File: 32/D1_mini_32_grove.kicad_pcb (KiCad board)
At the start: 2 copper layers, 3 parts, among them J1 Conn_01x04_Pin, J2 Conn_01x04_Pin, U1 esp32-wemos-d1-mini

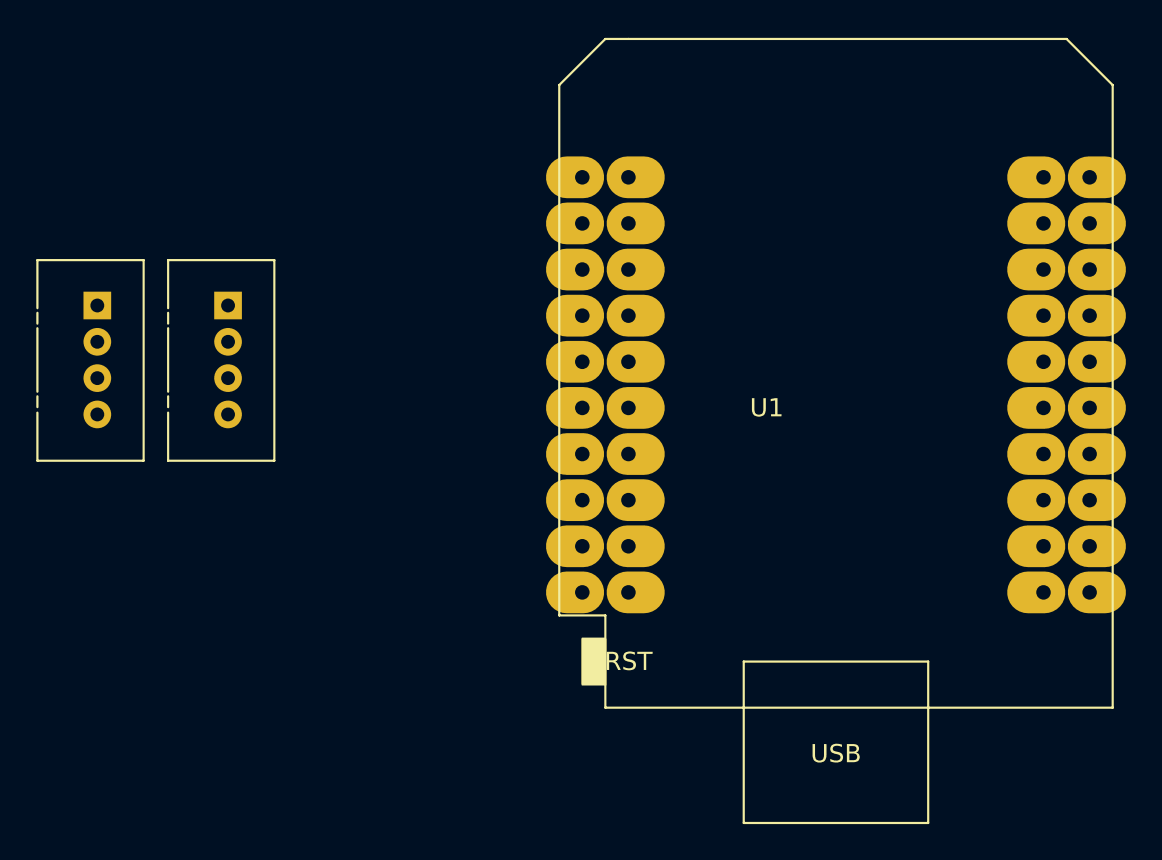
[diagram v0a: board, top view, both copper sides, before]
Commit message: First draft of 32 board ready for testrun
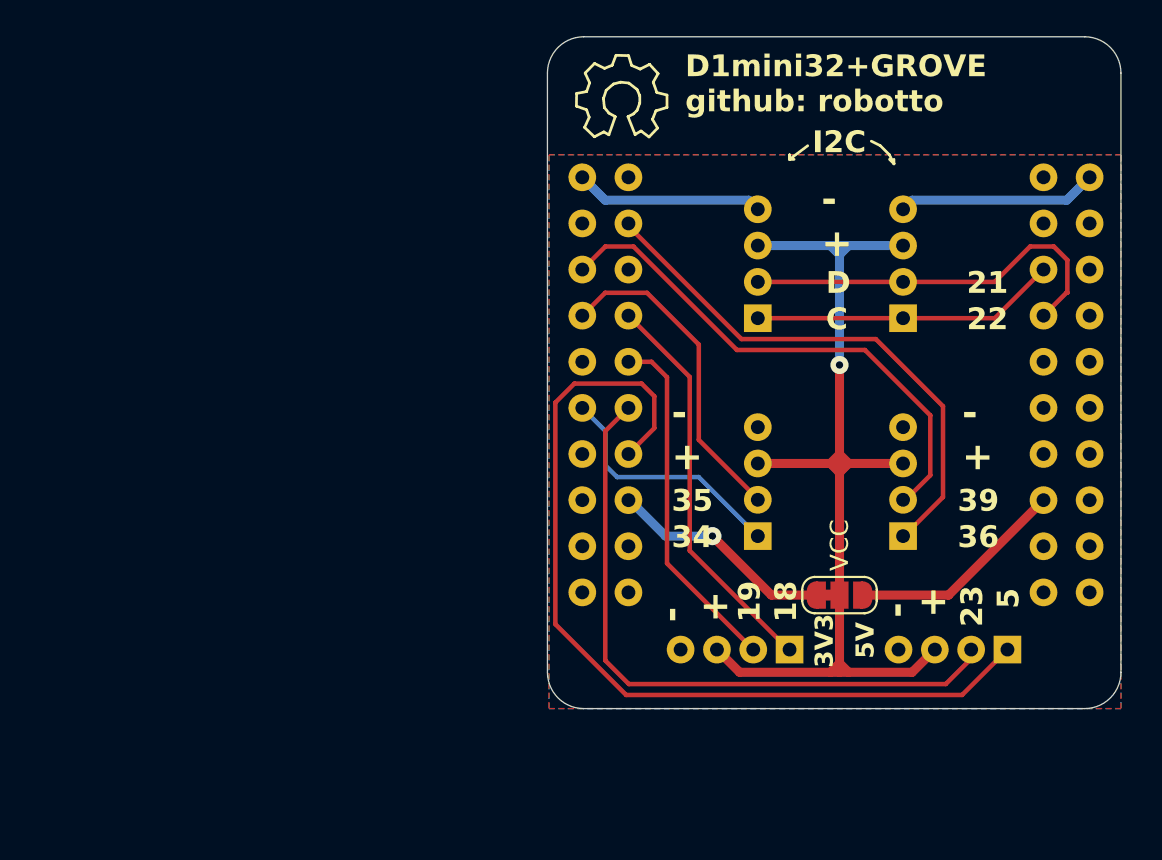
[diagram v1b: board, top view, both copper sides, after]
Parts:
- added ?: OSHW, pretty:OSHW, F.Cu at (101.0, 48.5)
- added J1: Conn_01x04_Pin, pretty:NS-Tech_Grove_1x04_P2mm_Vertical, F.Cu at (116.5, 72.5)
- added J2: Conn_01x04_Pin, pretty:NS-Tech_Grove_1x04_P2mm_Vertical, F.Cu at (108.5, 72.5)
- added J3: Conn_01x04_Pin, pretty:NS-Tech_Grove_1x04_P2mm_Vertical, F.Cu at (110.2, 78.8)
- added J4: Conn_01x04_Pin, pretty:NS-Tech_Grove_1x04_P2mm_Vertical, F.Cu at (122.2, 78.8)
- added VCC: SolderJumper_3_Bridged12, Jumper:SolderJumper-3_P1.3mm_Bridged12_RoundedPad1.0x1.5mm_NumberLabels, F.Cu at (113.0, 75.8)
- moved I2C_1 44.4 mm to (116.5, 60.5), turned to 180 degrees
- moved I2C_2 29.2 mm to (108.5, 60.5), turned to 180 degrees
- renumbered J1 to I2C_1, J2 to I2C_2
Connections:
- I2C_1 pad 1: +3.3V -> /SCL
- I2C_1 pad 2: GND -> /SDA
- I2C_1 pad 3: Net-(J1-Pin_3) -> VCC
- I2C_1 pad 4: Net-(J1-Pin_4) -> GND
- I2C_2 pad 1: +3.3V -> /SCL
- I2C_2 pad 2: GND -> /SDA
- I2C_2 pad 3: Net-(J1-Pin_3) -> VCC
- I2C_2 pad 4: Net-(J1-Pin_4) -> GND
- U1 pad 10: unconnected-(U1-IO_19/D6-Pad10) -> /IO19
- U1 pad 11: unconnected-(U1-IO_34-Pad11) -> /IO34
- U1 pad 12: unconnected-(U1-IO_23/D7-Pad12) -> /IO23
- U1 pad 14: unconnected-(U1-IO_05/D8-Pad14) -> /IO5
- U1 pad 25: Net-(J1-Pin_4) -> /SCL
- U1 pad 27: Net-(J1-Pin_3) -> /SDA
- U1 pad 35: unconnected-(U1-VCC_(USB)-Pad35) -> +5V
- U1 pad 4: unconnected-(U1-IO_36/SVP/A0-Pad4) -> /IO36
- U1 pad 5: unconnected-(U1-IO_39/SVN-Pad5) -> /IO39
- U1 pad 7: unconnected-(U1-IO_35-Pad7) -> /IO35
- U1 pad 8: unconnected-(U1-IO_18/D5-Pad8) -> /IO18
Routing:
- net VCC: track 0.00 -> 58.2 mm, vias 0 -> 1
- net /IO5: track 0.00 -> 49.7 mm
- net /IO23: track 0.00 -> 36.2 mm
- net /IO36: track 0.00 -> 29.6 mm
- net /IO39: track 0.00 -> 28.8 mm
- net /IO18: track 0.00 -> 22.1 mm
- net /SDA: track 0.00 -> 21.8 mm
- net GND: track 0.00 -> 21.4 mm
- net /IO19: track 0.00 -> 19.4 mm
- net /IO35: track 0.00 -> 18.1 mm
- net /SCL: track 0.00 -> 16.8 mm
- net /IO34: track 0.00 -> 13.7 mm
- net +3.3V: track 0.00 -> 12.5 mm, vias 0 -> 1
- net +5V: track 0.00 -> 12.1 mm
- added copper zone on B.Cu, net GND
- added copper zone on F.Cu, net GND
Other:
- board outline added: 31.6 x 37 mm
- rule pad_to_mask_clearance: 0 -> 0.2
- board text added: "+"
- board text added: "-"
- board text added: "- +"
- board text added: "18"
- board text added: "19"
- board text added: "21"
- board text added: "22"
- board text added: "23"
- board text added: "34"
- board text added: "35"
- board text added: "36"
- board text added: "39"
- board text added: "3V3"
- board text added: "5"
- board text added: "5V"
- board text added: "C"
- board text added: "D"
- board text added: "D1mini32+GROVE github: robotto"
- board text added: "I2C"
